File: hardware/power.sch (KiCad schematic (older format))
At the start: 4 parts

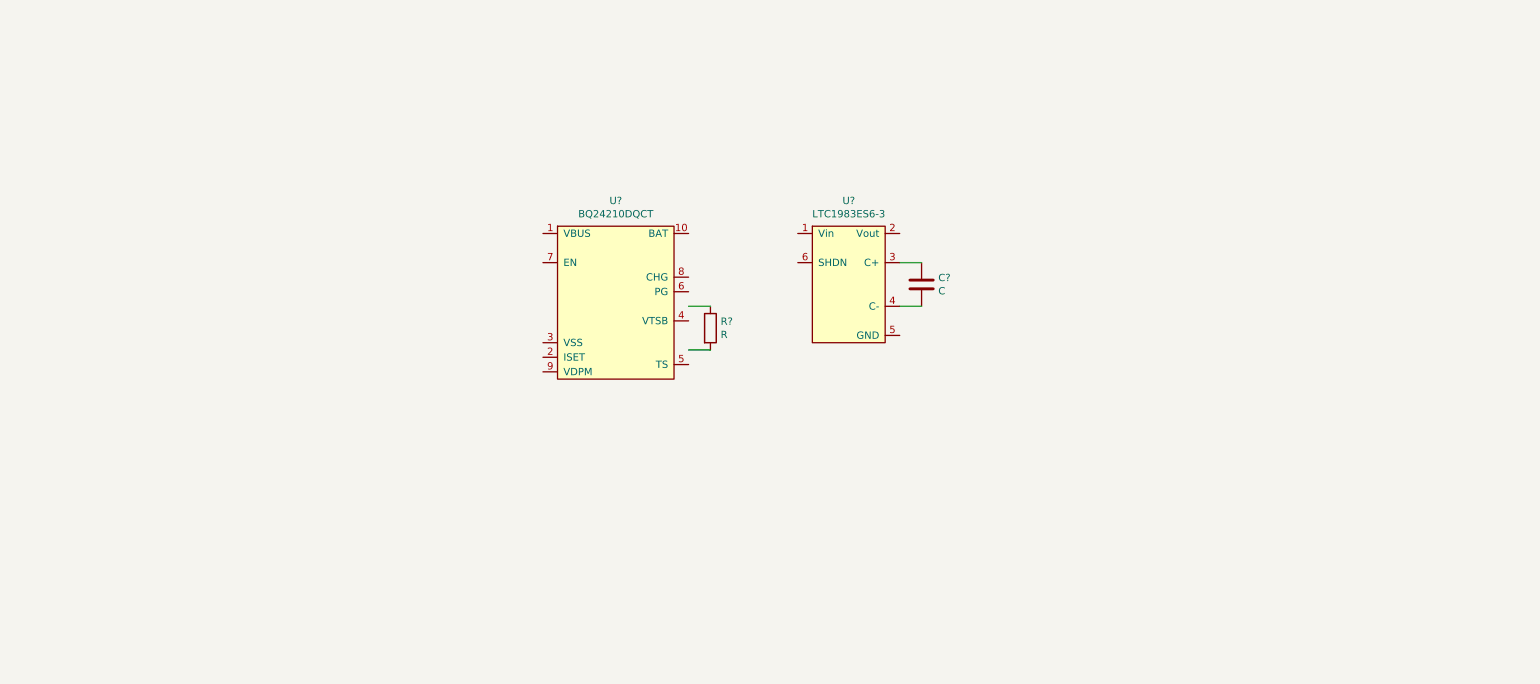
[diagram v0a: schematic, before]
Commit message: Create power.pro
created a schematic for the power system
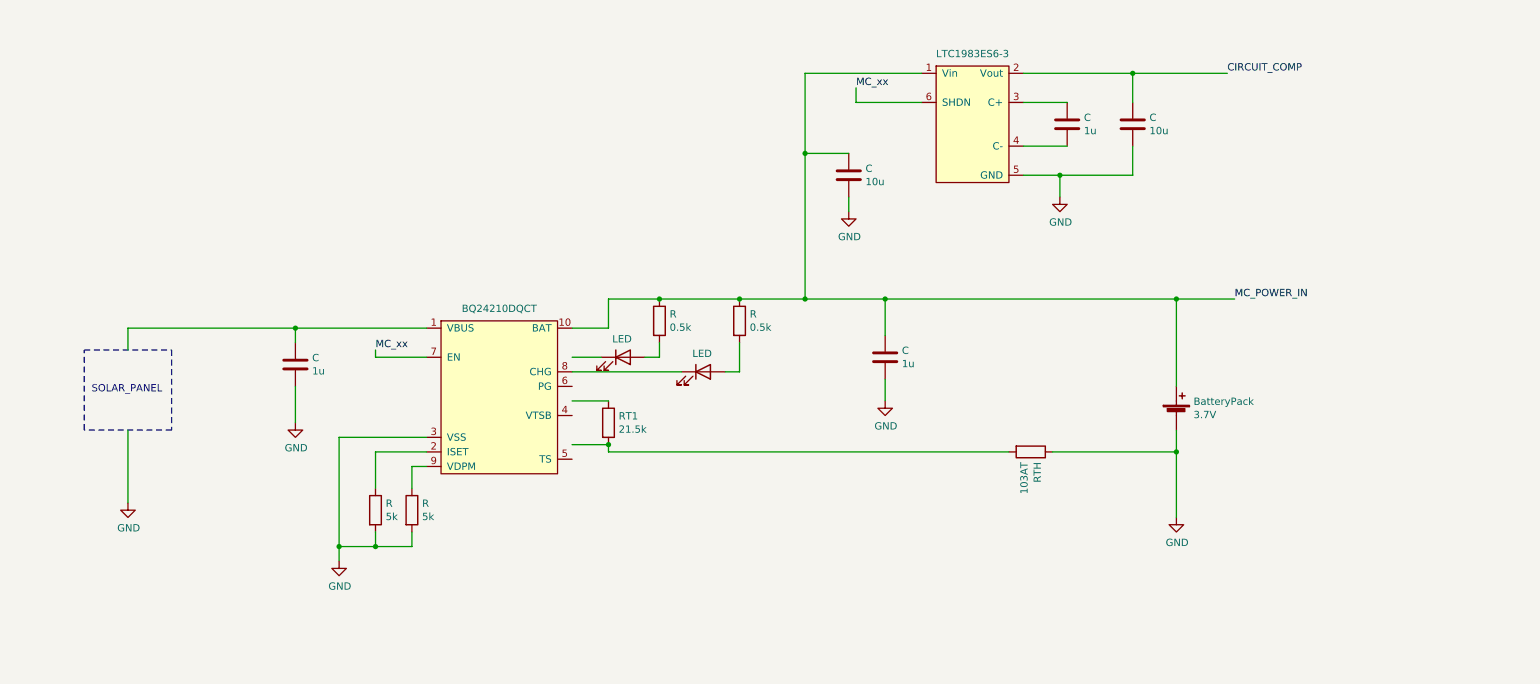
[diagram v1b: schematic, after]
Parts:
- added BatteryPack: 3.7V, symbol Device:Battery_Cell
- added C (x2): 10u, symbol Device:C
- added C (x2): 1u, symbol Device:C
- added D? (x2): LED, symbol Device:LED
- added R: 5k, symbol Device:R
- added R (x2): 0.5k, symbol Device:R
- added RT1: 21.5k, symbol Device:R
- added RTH: 103AT, symbol Device:R
- C: renamed from C?; value C -> 1u
- R: renamed from R?; value R -> 5k
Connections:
- net labels added: CIRCUIT_COMP, GND, MC_POWER_IN, MC_xx
- wire segments 4 -> 59
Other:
- note added: "SOLAR_PANEL"
- moved on the sheet: C, R

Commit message: added blocking diode
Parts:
- added D?: DIODE, symbol Simulation_SPICE:DIODE
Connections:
- wire segments 59 -> 60
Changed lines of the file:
@@
 $Descr A4 11693 8268
 encoding utf-8
-Sheet 1 4
+Sheet 1 1
 Title "Power Schematic"
 Date "2021-07-27"
@@
 	1450 4400 1450 3900
 Wire Wire Line
-	2600 3200 1450 3200
-Wire Wire Line
 	1450 3200 1450 3350
-Connection ~ 2600 3200
 $Comp
 L Device:R R
@@
 Wire Wire Line
 	6400 2300 6400 2400
+Wire Wire Line
+	1900 3200 1450 3200
+$Comp
+L Simulation_SPICE:DIODE D?
+U 1 1 610C81D5
+P 2050 3200
+F 0 "D?" H 2050 3417 50  0001 C CNN
+F 1 "DIODE" H 2050 3325 50  0000 C CNN
+F 2 "" H 2050 3200 50  0001 C CNN
+F 3 "~" H 2050 3200 50  0001 C CNN
+F 4 "Y" H 2050 3200 50  0001 L CNN "Spice_Netlist_Enabled"
+F 5 "D" H 2050 3200 50  0001 L CNN "Spice_Primitive"
+	1    2050 3200
+	1    0    0    -1
+$EndComp
+Wire Wire Line
+	2600 3200 2200 3200
+Connection ~ 2600 3200
 $EndSCHEMATC

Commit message: Added all Digikey part numbers. Started MC schematic. Fixed the reference number on some symbols.
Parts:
- removed C (x3): 1u, symbol Device:C
- removed C (x2): 10u, symbol Device:C
- removed D?: DIODE, symbol Simulation_SPICE:DIODE
- removed R (x2): 5k, symbol Device:R
- removed R (x2): 0.5k, symbol Device:R
- removed RT1: 21.5k, symbol Device:R
- removed RTH: 103AT, symbol Device:R
- removed U?: BQ24210DQCT, Package_SON:WSON-10-1EP_2x3mm_P0.5mm_EP0.84x2.4mm, symbol mallard:BQ24210DQCT
- removed U?: LTC1983ES6-3, Package_TO_SOT_SMD:SOT-23-6, symbol mallard:LTC1983ES6-3
- added C10, C7, C9: 1uF, symbol Device:C
- added C11, C8: 10uF, symbol Device:C
- added R12, R13: 5.1k, symbol Device:R
- added R14: 21.5k, symbol Device:R
- added R15, R16: 510, symbol Device:R
- added TH1: 103AT, symbol Device:Thermistor
- added U5: BQ24210DQCT, Package_SON:WSON-10-1EP_2x3mm_P0.5mm_EP0.84x2.4mm, symbol mallard:BQ24210DQCT
- added U6: LTC1983ES6-3, Package_TO_SOT_SMD:SOT-23-6, symbol mallard:LTC1983ES6-3
- gave numbers to parts that had none: 2
- renumbered BatteryPack to BatteryPack1
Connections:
- net labels added: +3V3
- net labels removed: MC_POWER_IN
- wire segments 60 -> 59

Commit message: Finished MC design
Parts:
- added D?: D, symbol Device:D
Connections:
- net labels added: -3V3, -3V3_SHDN_L, Charge_EN
- net labels removed: CIRCUIT_COMP, MC_xx
- wire segments 59 -> 57
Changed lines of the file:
@@
 Wire Wire Line
 	4500 4000 4750 4000
-Text Label 6450 1550 0    50   ~ 0
-MC_xx
-Wire Wire Line
-	6900 1650 6450 1650
-Wire Wire Line
-	6450 1650 6450 1550
 Wire Wire Line
 	6900 1450 6100 1450
@@
 	6100 1450 6100 2000
 Connection ~ 6100 3000
-Text Label 9000 1450 0    50   ~ 0
-CIRCUIT_COMP
 Wire Wire Line
 	8350 1450 9000 1450
@@
 	8650 3000 6650 3000
 Connection ~ 6650 3000
-Text Label 3150 3350 0    50   ~ 0
-MC_xx
-Wire Wire Line
-	3500 3400 3150 3400
-Wire Wire Line
-	3150 3400 3150 3350
 Wire Notes Line
 	1750 3350 1750 3900
@@
 Wire Wire Line
 	5650 3000 6100 3000
+Wire Wire Line
+	3500 3400 3400 3400
+Text GLabel 3400 3400 0    50   Input ~ 0
+Charge_EN
+$Comp
+L Device:D D?
+U 1 1 6161D676
+P 2050 3200
+F 0 "D?" H 2050 2984 50  0000 C CNN
+F 1 "D" H 2050 3075 50  0000 C CNN
+F 2 "" H 2050 3200 50  0001 C CNN
+F 3 "~" H 2050 3200 50  0001 C CNN
+	1    2050 3200
+	-1   0    0    1
+$EndComp
+Text GLabel 6800 1650 0    50   Input ~ 0
+-3V3_SHDN_L
+Wire Wire Line
+	6900 1650 6800 1650
+$Comp
+L power:-3V3 #PWR?
+U 1 1 6161FA5E
+P 9000 1450
+F 0 "#PWR?" H 9000 1550 50  0001 C CNN
+F 1 "-3V3" V 9015 1578 50  0000 L CNN
+F 2 "" H 9000 1450 50  0001 C CNN
+F 3 "" H 9000 1450 50  0001 C CNN
+	1    9000 1450
+	0    1    1    0
+$EndComp
 $EndSCHEMATC

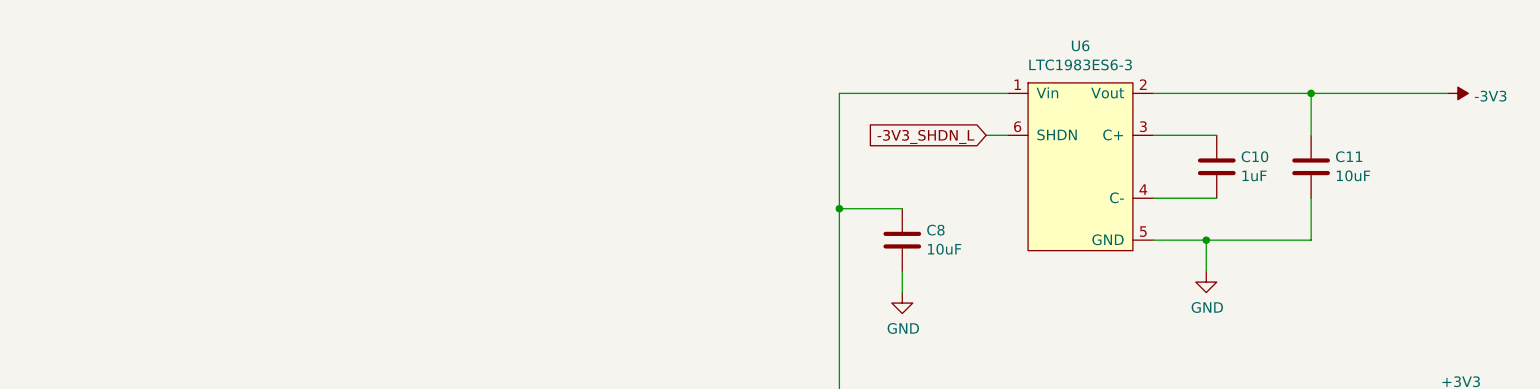
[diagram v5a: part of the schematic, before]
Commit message: Added 1V LDO. Added LDO symbol
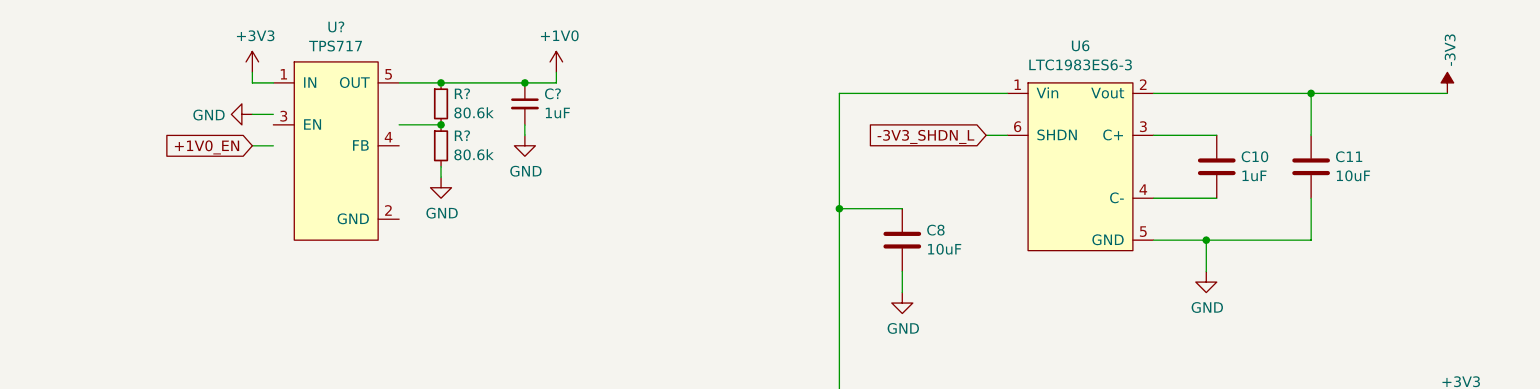
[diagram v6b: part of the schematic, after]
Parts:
- added C?: 1uF, symbol Device:C_Small
- added R? (x2): 80.6k, symbol Device:R_Small
- added U?: TPS717, symbol mallard:TPS717
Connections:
- net labels added: +1V0, +1V0_EN
- wire segments 57 -> 68
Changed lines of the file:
@@
 F 3 "" H 9000 1450 50  0001 C CNN
 	1    9000 1450
+	1    0    0    -1
+$EndComp
+$Comp
+L power:+3V3 #PWR?
+U 1 1 615B9B0D
+P 3300 1350
+F 0 "#PWR?" H 3300 1200 50  0001 C CNN
+F 1 "+3V3" H 3315 1523 50  0000 C CNN
+F 2 "" H 3300 1350 50  0001 C CNN
+F 3 "" H 3300 1350 50  0001 C CNN
+	1    3300 1350
+	1    0    0    -1
+$EndComp
+Wire Wire Line
+	3400 1400 3300 1400
+Wire Wire Line
+	3300 1400 3300 1350
+$Comp
+L power:GND #PWR?
+U 1 1 615BBB45
+P 3300 1550
+F 0 "#PWR?" H 3300 1300 50  0001 C CNN
+F 1 "GND" V 3305 1422 50  0000 R CNN
+F 2 "" H 3300 1550 50  0001 C CNN
+F 3 "" H 3300 1550 50  0001 C CNN
+	1    3300 1550
 	0    1    1    0
 $EndComp
+Wire Wire Line
+	3400 1550 3300 1550
+Text GLabel 3300 1700 0    50   Input ~ 0
++1V0_EN
+Wire Wire Line
+	3300 1700 3400 1700
+Wire Wire Line
+	4000 1400 4200 1400
+$Comp
+L Device:R_Small R?
+U 1 1 615C0490
+P 4200 1500
+F 0 "R?" H 4259 1546 50  0000 L CNN
+F 1 "80.6k" H 4259 1455 50  0000 L CNN
+F 2 "" H 4200 1500 50  0001 C CNN
+F 3 "~" H 4200 1500 50  0001 C CNN
+	1    4200 1500
+	1    0    0    -1
+$EndComp
+$Comp
+L mallard:TPS717 U?
+U 1 1 615C2667
+P 3700 1300
+F 0 "U?" H 3700 1465 50  0000 C CNN
+F 1 "TPS717" H 3700 1374 50  0000 C CNN
+F 2 "" H 3650 1750 50  0001 C CNN
+F 3 "" H 3650 1750 50  0001 C CNN
+F 4 "296-27043-1-ND" H 3700 1300 50  0001 C CNN "Digikey"
+	1    3700 1300
+	1    0    0    -1
+$EndComp
+Wire Wire Line
+	4200 1600 4000 1600
+$Comp
+L Device:R_Small R?
+U 1 1 615C475F
+P 4200 1700
+F 0 "R?" H 4259 1746 50  0000 L CNN
+F 1 "80.6k" H 4259 1655 50  0000 L CNN
+F 2 "" H 4200 1700 50  0001 C CNN
+F 3 "~" H 4200 1700 50  0001 C CNN
+	1    4200 1700
+	1    0    0    -1
+$EndComp
+Connection ~ 4200 1600
+$Comp
+L power:GND #PWR?
+U 1 1 615C4B04
+P 4200 1850
+F 0 "#PWR?" H 4200 1600 50  0001 C CNN
+F 1 "GND" H 4205 1677 50  0000 C CNN
+F 2 "" H 4200 1850 50  0001 C CNN
+F 3 "" H 4200 1850 50  0001 C CNN
+	1    4200 1850
+	1    0    0    -1
+$EndComp
+Wire Wire Line
+	4200 1800 4200 1850
+Wire Wire Line
+	4200 1400 4600 1400
+Connection ~ 4200 1400
+$Comp
+L Device:C_Small C?
+U 1 1 615C874E
+P 4600 1500
+F 0 "C?" H 4692 1546 50  0000 L CNN
+F 1 "1uF" H 4692 1455 50  0000 L CNN
+F 2 "" H 4600 1500 50  0001 C CNN
+F 3 "~" H 4600 1500 50  0001 C CNN
+	1    4600 1500
+	1    0    0    -1
+$EndComp
+$Comp
+L power:GND #PWR?
+U 1 1 615C9273
+P 4600 1650
+F 0 "#PWR?" H 4600 1400 50  0001 C CNN
+F 1 "GND" H 4605 1477 50  0000 C CNN
+F 2 "" H 4600 1650 50  0001 C CNN
+F 3 "" H 4600 1650 50  0001 C CNN
+	1    4600 1650
+	1    0    0    -1
+$EndComp
+Wire Wire Line
+	4600 1600 4600 1650
+Wire Wire Line
+	4600 1400 4750 1400
+Wire Wire Line
+	4750 1400 4750 1350
+Connection ~ 4600 1400
+$Comp
+L power:+1V0 #PWR?
+U 1 1 615CDF04
+P 4750 1350
+F 0 "#PWR?" H 4750 1200 50  0001 C CNN
+F 1 "+1V0" H 4765 1523 50  0000 C CNN
+F 2 "" H 4750 1350 50  0001 C CNN
+F 3 "" H 4750 1350 50  0001 C CNN
+	1    4750 1350
+	1    0    0    -1
+$EndComp
 $EndSCHEMATC

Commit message: Not sure what changes I made sry
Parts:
- removed R16: 510, symbol Device:R
- added C?: 1uF, symbol Device:C_Small
- added R?: Jumper, symbol Device:R_Small
- added R?: 3.6k, symbol Device:R
- C?: Digikey (none) -> 311-1446-1-ND
- R15: value 510 -> 3.6k; Digikey CR0603-FX-5100ELFCT-ND -> P3.6KGCT-ND
- R?: Digikey (none) -> RMCF0603FT80K6CT-ND
- R?: value 80.6k -> 324k; Digikey (none) -> P324KHCT-ND
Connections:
- wire segments 68 -> 70
- no-connect marks 0 -> 2
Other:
- note added: "DNI VDPM Resistor"
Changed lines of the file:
@@
 P 5100 3150
 F 0 "R15" H 5170 3196 50  0000 L CNN
-F 1 "510" H 5170 3105 50  0000 L CNN
+F 1 "3.6k" H 5170 3105 50  0000 L CNN
 F 2 "" V 5030 3150 50  0001 C CNN
 F 3 "~" H 5100 3150 50  0001 C CNN
-F 4 "CR0603-FX-5100ELFCT-ND" H 5100 3150 50  0001 C CNN "Digikey"
+F 4 "P3.6KGCT-ND" H 5100 3150 50  0001 C CNN "Digikey"
 	1    5100 3150
 	1    0    0    -1
@@
 	8650 4000 8650 4500
 Wire Wire Line
-	5100 3000 5650 3000
-$Comp
-L Device:R R16
-U 1 1 615CDE99
-P 5650 3150
-F 0 "R16" H 5720 3196 50  0000 L CNN
-F 1 "510" H 5720 3105 50  0000 L CNN
-F 2 "" V 5580 3150 50  0001 C CNN
-F 3 "~" H 5650 3150 50  0001 C CNN
-F 4 "CR0603-FX-5100ELFCT-ND" H 5650 3150 50  0001 C CNN "Digikey"
-	1    5650 3150
-	1    0    0    -1
-$EndComp
-Connection ~ 5650 3000
-Wire Wire Line
-	5650 3000 6100 3000
-Wire Wire Line
 	3500 3400 3400 3400
 Text GLabel 3400 3400 0    50   Input ~ 0
@@
 F 3 "" H 9000 1450 50  0001 C CNN
 	1    9000 1450
-	1    0    0    -1
-$EndComp
-$Comp
-L power:+3V3 #PWR?
-U 1 1 615B9B0D
-P 3300 1350
-F 0 "#PWR?" H 3300 1200 50  0001 C CNN
-F 1 "+3V3" H 3315 1523 50  0000 C CNN
-F 2 "" H 3300 1350 50  0001 C CNN
-F 3 "" H 3300 1350 50  0001 C CNN
-	1    3300 1350
-	1    0    0    -1
-$EndComp
-Wire Wire Line
-	3400 1400 3300 1400
-Wire Wire Line
-	3300 1400 3300 1350
+	0    1    1    0
+$EndComp
 $Comp
 L power:GND #PWR?
 U 1 1 615BBB45
-P 3300 1550
-F 0 "#PWR?" H 3300 1300 50  0001 C CNN
-F 1 "GND" V 3305 1422 50  0000 R CNN
-F 2 "" H 3300 1550 50  0001 C CNN
-F 3 "" H 3300 1550 50  0001 C CNN
-	1    3300 1550
+P 2850 1550
+F 0 "#PWR?" H 2850 1300 50  0001 C CNN
+F 1 "GND" V 2855 1422 50  0000 R CNN
+F 2 "" H 2850 1550 50  0001 C CNN
+F 3 "" H 2850 1550 50  0001 C CNN
+	1    2850 1550
 	0    1    1    0
 $EndComp
-Wire Wire Line
-	3400 1550 3300 1550
 Text GLabel 3300 1700 0    50   Input ~ 0
 +1V0_EN
@@
 F 2 "" H 4200 1500 50  0001 C CNN
 F 3 "~" H 4200 1500 50  0001 C CNN
+F 4 "RMCF0603FT80K6CT-ND" H 4200 1500 50  0001 C CNN "Digikey"
 	1    4200 1500
 	1    0    0    -1
@@
 F 1 "TPS717" H 3700 1374 50  0000 C CNN
 F 2 "" H 3650 1750 50  0001 C CNN
-F 3 "" H 3650 1750 50  0001 C CNN
+F 3 "https://www.ti.com/lit/ds/symlink/tps717.pdf?HQS=dis-dk-null-digikeymode-dsf-pf-null-wwe&ts=1633366861578&ref_url=https%253A%252F%252Fwww.ti.com%252Fgeneral%252Fdocs%252Fsuppproductinfo.tsp%253FdistId%253D10%2526gotoUrl%253Dhttps%253A%252F%252Fwww.ti.com%252Flit%252Fgpn%252Ftps717" H 3650 1750 50  0001 C CNN
 F 4 "296-27043-1-ND" H 3700 1300 50  0001 C CNN "Digikey"
 	1    3700 1300
@@
 P 4200 1700
 F 0 "R?" H 4259 1746 50  0000 L CNN
-F 1 "80.6k" H 4259 1655 50  0000 L CNN
+F 1 "324k" H 4259 1655 50  0000 L CNN
 F 2 "" H 4200 1700 50  0001 C CNN
 F 3 "~" H 4200 1700 50  0001 C CNN
+F 4 "P324KHCT-ND" H 4200 1700 50  0001 C CNN "Digikey"
 	1    4200 1700
 	1    0    0    -1
@@
 Wire Wire Line
 	4200 1800 4200 1850
-Wire Wire Line
-	4200 1400 4600 1400
 Connection ~ 4200 1400
-$Comp
-L Device:C_Small C?
-U 1 1 615C874E
-P 4600 1500
-F 0 "C?" H 4692 1546 50  0000 L CNN
-F 1 "1uF" H 4692 1455 50  0000 L CNN
-F 2 "" H 4600 1500 50  0001 C CNN
-F 3 "~" H 4600 1500 50  0001 C CNN
-	1    4600 1500
-	1    0    0    -1
-$EndComp
 $Comp
 L power:GND #PWR?
@@
 Wire Wire Line
 	4600 1600 4600 1650
-Wire Wire Line
-	4600 1400 4750 1400
-Wire Wire Line
-	4750 1400 4750 1350
-Connection ~ 4600 1400
 $Comp
 L power:+1V0 #PWR?
 U 1 1 615CDF04
-P 4750 1350
-F 0 "#PWR?" H 4750 1200 50  0001 C CNN
-F 1 "+1V0" H 4765 1523 50  0000 C CNN
-F 2 "" H 4750 1350 50  0001 C CNN
-F 3 "" H 4750 1350 50  0001 C CNN
-	1    4750 1350
-	1    0    0    -1
-$EndComp
+P 5100 1400
+F 0 "#PWR?" H 5100 1250 50  0001 C CNN
+F 1 "+1V0" H 5115 1573 50  0000 C CNN
+F 2 "" H 5100 1400 50  0001 C CNN
+F 3 "" H 5100 1400 50  0001 C CNN
+	1    5100 1400
+	1    0    0    -1
+$EndComp
+$Comp
+L Device:R_Small R?
+U 1 1 615D2E50
+P 4900 1400
+F 0 "R?" V 4704 1400 50  0000 C CNN
+F 1 "Jumper" V 4795 1400 50  0000 C CNN
+F 2 "" H 4900 1400 50  0001 C CNN
+F 3 "~" H 4900 1400 50  0001 C CNN
+F 4 "541-0.0SBCT-ND" V 4900 1400 50  0001 C CNN "Digikey"
+	1    4900 1400
+	0    1    1    0
+$EndComp
+Wire Wire Line
+	5000 1400 5100 1400
+Wire Wire Line
+	3400 1400 3400 1350
+Wire Wire Line
+	3400 1350 3050 1350
+Wire Wire Line
+	3050 1350 3050 1250
+$Comp
+L power:+3V3 #PWR?
+U 1 1 615DFBEC
+P 3050 1250
+F 0 "#PWR?" H 3050 1100 50  0001 C CNN
+F 1 "+3V3" H 3065 1423 50  0000 C CNN
+F 2 "" H 3050 1250 50  0001 C CNN
+F 3 "" H 3050 1250 50  0001 C CNN
+	1    3050 1250
+	1    0    0    -1
+$EndComp
+NoConn ~ 3400 4400
+NoConn ~ 3400 4500
+Text Notes 3500 4650 0    50   ~ 0
+DNI VDPM Resistor
+Wire Wire Line
+	3050 1550 2850 1550
+Wire Wire Line
+	3400 1550 3050 1550
+Connection ~ 3050 1550
+Connection ~ 3050 1350
+$Comp
+L Device:C_Small C?
+U 1 1 615D8D82
+P 3050 1450
+F 0 "C?" H 3142 1496 50  0000 L CNN
+F 1 "1uF" H 3142 1405 50  0000 L CNN
+F 2 "" H 3050 1450 50  0001 C CNN
+F 3 "~" H 3050 1450 50  0001 C CNN
+F 4 "311-1446-1-ND" H 3050 1450 50  0001 C CNN "Digikey"
+	1    3050 1450
+	1    0    0    -1
+$EndComp
+Wire Wire Line
+	4600 1400 4800 1400
+Wire Wire Line
+	4200 1400 4600 1400
+Connection ~ 4600 1400
+$Comp
+L Device:C_Small C?
+U 1 1 615C874E
+P 4600 1500
+F 0 "C?" H 4692 1546 50  0000 L CNN
+F 1 "1uF" H 4692 1455 50  0000 L CNN
+F 2 "" H 4600 1500 50  0001 C CNN
+F 3 "~" H 4600 1500 50  0001 C CNN
+F 4 "311-1446-1-ND" H 4600 1500 50  0001 C CNN "Digikey"
+	1    4600 1500
+	1    0    0    -1
+$EndComp
+Wire Wire Line
+	5100 3000 5650 3000
+$Comp
+L Device:R R?
+U 1 1 615E6A6B
+P 5650 3150
+F 0 "R?" H 5720 3196 50  0000 L CNN
+F 1 "3.6k" H 5720 3105 50  0000 L CNN
+F 2 "" V 5580 3150 50  0001 C CNN
+F 3 "~" H 5650 3150 50  0001 C CNN
+F 4 "P3.6KGCT-ND" H 5650 3150 50  0001 C CNN "Digikey"
+	1    5650 3150
+	1    0    0    -1
+$EndComp
+Connection ~ 5650 3000
+Wire Wire Line
+	5650 3000 6100 3000
 $EndSCHEMATC
